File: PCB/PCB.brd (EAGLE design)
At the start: 215 parts, among them J3 Boot, Q1 FS8205A, U1 ESP32-S3HOLE

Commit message: Created the Led hole for keys library.
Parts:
- added U$97: WS2812B, Led-WS2812B:WS2812B
- moved LED1 3.80 mm to (358.8, 109.9)
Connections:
- new net LED_GND: U$97.GND
- new net LED_VDD: U$97.VDD
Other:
- board outline added: 428.5 x 124 mm
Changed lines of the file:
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@@
 <circle x="412.745" y="48.175" radius="2" width="0.001" layer="48"/>
 <circle x="428" y="48.175" radius="1.5" width="0.001" layer="48"/>
+<wire x1="4.5" y1="127" x2="429" y2="127" width="0.01" layer="20"/>
+<wire x1="431" y1="125" x2="431" y2="5" width="0.01" layer="20"/>
+<wire x1="4.6" y1="3" x2="2.5" y2="5" width="0.01" layer="20" curve="-92.862405"/>
+<wire x1="2.5" y1="5" x2="2.5" y2="125" width="0.01" layer="20"/>
+<wire x1="2.5" y1="125" x2="4.5" y2="127" width="0.01" layer="20" curve="-90"/>
+<wire x1="429" y1="127" x2="431" y2="125" width="0.01" layer="20" curve="-90"/>
+<wire x1="431" y1="5" x2="429" y2="3" width="0.01" layer="20" curve="-90"/>
+<wire x1="429" y1="3" x2="4.6" y2="3" width="0.01" layer="20"/>
 </plain>
 <attributes>
@@
 <attribute name="VALUE" x="308.85" y="107.123" size="1.27" layer="27" align="top-left"/>
 </element>
-<element name="LED1" library="SMD5050 LED" package="LED5050_W" value="" x="355" y="110" smashed="yes">
-<attribute name="NAME" x="353.095" y="112.894" size="0.8128" layer="25" ratio="18"/>
-<attribute name="VALUE" x="353.222" y="106.625" size="0.4064" layer="27" ratio="10"/>
+<element name="LED1" library="SMD5050 LED" package="LED5050_W" value="" x="358.8" y="109.9" smashed="yes">
+<attribute name="NAME" x="356.895" y="112.794" size="0.8128" layer="25" ratio="18"/>
+<attribute name="VALUE" x="357.022" y="106.525" size="0.4064" layer="27" ratio="10"/>
 </element>
 <element name="USB" library="con-headers-jp" package="SIP-100-04-32" value="F-1X04-SIP-100-32" x="375" y="115" smashed="yes" rot="R90">
@@
 <attribute name="PROD_ID" value="RES-12181" x="-18" y="-51.7" size="1.778" layer="27" display="off"/>
 <attribute name="VALUE" x="-18" y="-52.716" size="0.6096" layer="27" font="vector" ratio="20" align="top-center"/>
+</element>
+<element name="U$97" library="Led-WS2812B" package="WS2812B" value="WS2812B" x="367.5" y="103.8" smashed="yes">
+<attribute name="NAME" x="366.4" y="102.2" size="0.254" layer="25"/>
+<attribute name="VALUE" x="366.4" y="105.2" size="0.254" layer="25"/>
 </element>
 </elements>
@@
 <contactref element="U$94" pad="18"/>
 <contactref element="U$94" pad="19"/>
-<wire x1="335.4488" y1="114.8606" x2="352.3" y2="111.65" width="0" layer="19" extent="1-1"/>
+<wire x1="335.4488" y1="114.8606" x2="356.1" y2="111.55" width="0" layer="19" extent="1-1"/>
 <wire x1="335.95" y1="123.1" x2="335.4488" y2="114.8606" width="0" layer="19" extent="1-1"/>
 <wire x1="319.355" y1="114.465" x2="335.4488" y2="114.8606" width="0" layer="19" extent="1-1"/>
@@
 <contactref element="USB" pad="1"/>
 </signal>
+<signal name="LED_VDD">
+<contactref element="U$97" pad="VDD"/>
+</signal>
+<signal name="LED_GND">
+<contactref element="U$97" pad="GND"/>
+</signal>
 </signals>

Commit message: Make the connections for the Battery and Power circuits
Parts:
- removed LED1: (no value), SMD5050 LED:LED5050_W
- removed U$97: WS2812B, Led-WS2812B:WS2812B
- added BATTERY: F-1X02-SIP-100-40, con-headers-jp:SIP-100-02-40
- C1, C2, C3: value RDE5C1H273J2M1H03A -> 1uF
- moved C3 459.5 mm to (418.9, 101.9), flipped to the bottom, turned to 180 degrees
- moved R3 455.3 mm to (411.8, 98.5), turned to 180 degrees
- moved R2 451.8 mm to (402.3, 117.8), turned to 90 degrees
- moved C2 449.2 mm to (409.9, 107.4), flipped to the bottom
- moved R1 445.4 mm to (400.5, 108.4), turned to 180 degrees
- moved Q1 444.3 mm to (416.5, 117.0), flipped to the bottom, turned to 180 degrees
- moved U$95 442.2 mm to (418.8, 109.5), flipped to the bottom, turned to 180 degrees
- moved C1 436.0 mm to (401.0, 101.9), flipped to the bottom, turned to 180 degrees
- moved U$96 435.9 mm to (407.8, 116.9), flipped to the bottom, turned to 180 degrees
- moved U1 82.0 mm to (330.0, 114.0)
- moved USB 43.7 mm to (417.9, 123.1), turned to 0 degrees
- moved R5 25.9 mm to (356.2, 109.8)
- moved BUTTON 10.6 mm to (348.9, 109.7), turned to 90 degrees
- moved U$94 8.54 mm to (306.7, 112.1)
- moved J3 8.40 mm to (350.7, 122.9), turned to 180 degrees
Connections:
- removed net INGND: USB.1
- removed net LED_GND: U$97.GND
- removed net LED_VDD: U$97.VDD
- removed net VDD: LED1.1-VDD
- new net B-: BATTERY.1, C2.1, Q1.2, Q1.3, U$96.6
- new net CHRG: U$95.7
- new net N$31: R1.P$1, U$95.2
- new net N$32: R2.P$2, U$96.2
- new net N$33: Q1.5, U$96.3
- new net N$34: Q1.4, U$96.1
- new net N$36: C2.2, R3.P$2, U$96.5
- new net STDBY: U$95.6
- net GND: now also C1.1, C3.1, Q1.6, Q1.7, R1.P$2, R2.P$1, U$95.1, U$95.3, USB.1; no longer LED1.3-GND
- net INVCC: now also C1.2, U$95.4, U$95.8
- net VCC: now also BATTERY.2, C3.2, R3.P$1, U$95.5

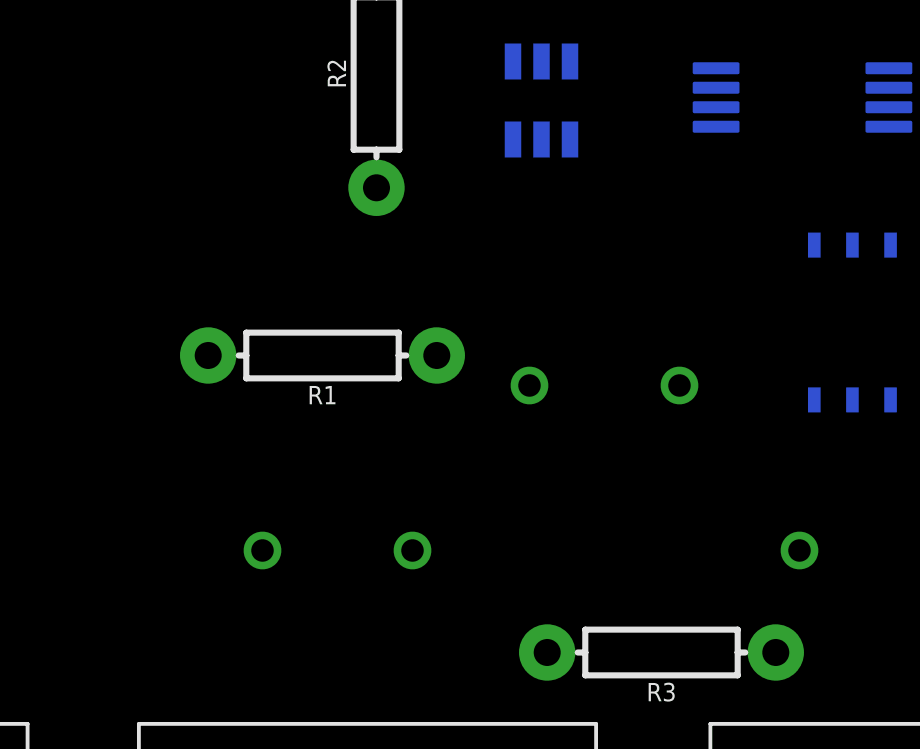
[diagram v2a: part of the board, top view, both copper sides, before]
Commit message: Make the screen DXF and added it to .pcb board
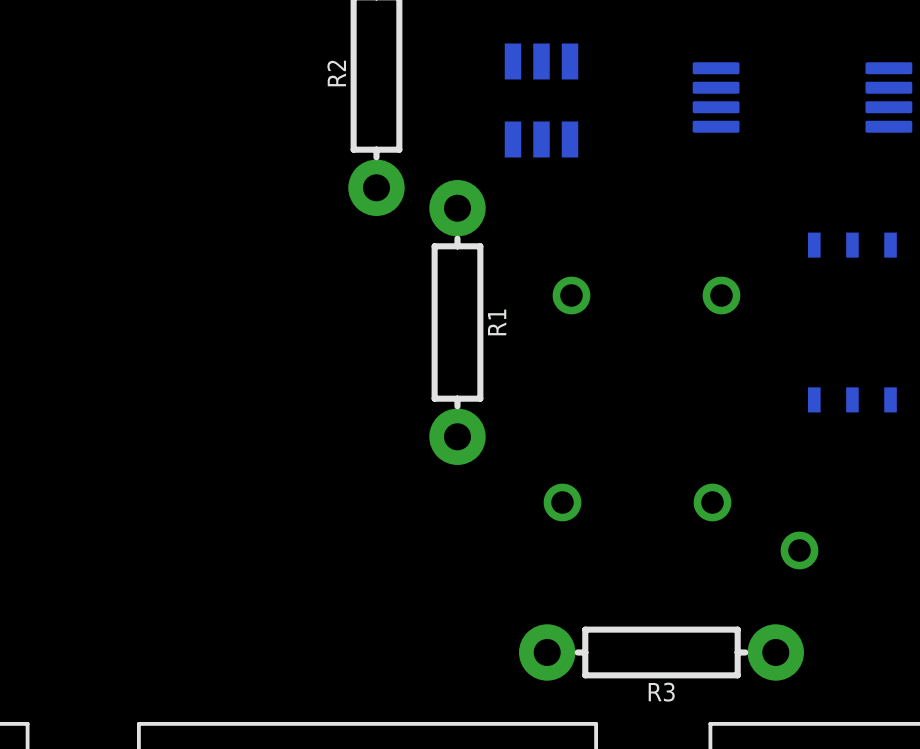
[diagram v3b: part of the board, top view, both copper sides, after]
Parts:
- moved C1 10.1 mm to (411.0, 103.5)
- moved R1 4.63 mm to (405.0, 109.5), turned to 270 degrees
- moved C2 3.31 mm to (411.3, 110.4)

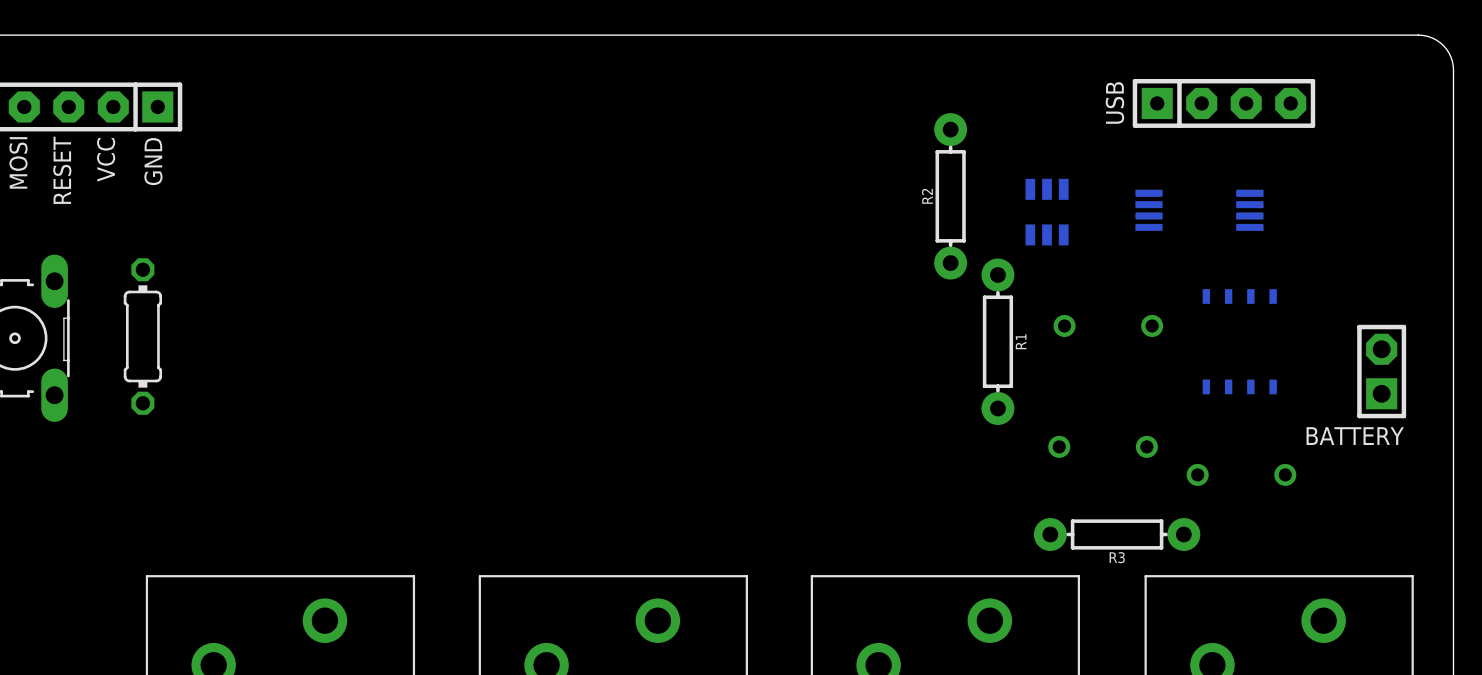
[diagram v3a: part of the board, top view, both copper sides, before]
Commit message: Changed Capacitor and resistor type
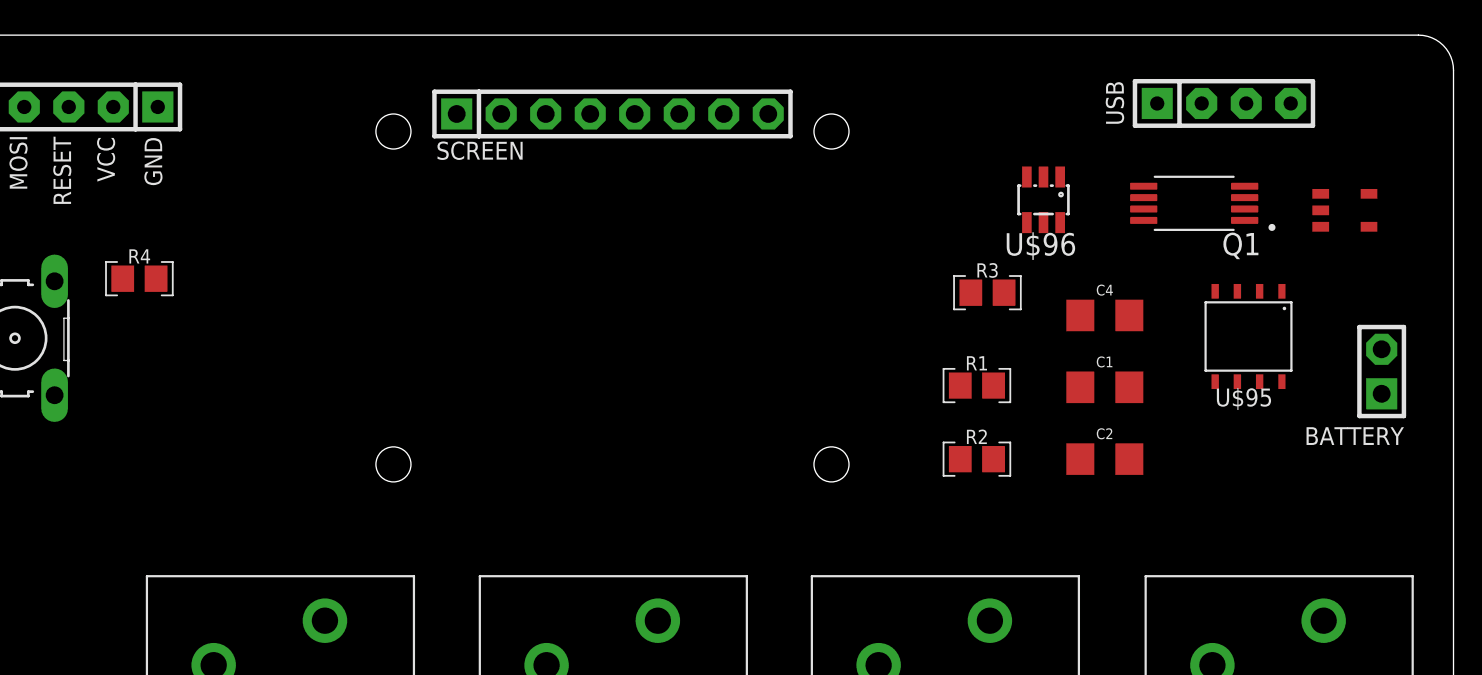
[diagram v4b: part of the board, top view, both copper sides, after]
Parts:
- removed C3: 1uF, Capacitor:CAP_RDE5C1H273J2M1H03A
- removed R5: 10K, rcl:0204/7
- added C4: 1.0uF, SparkFun-Capacitors:1206
- added R4: 1K, resistors:R-0805
- added REGULATOR: RT9080-33GJ5, RT9080:TSOT-23-5_RIT
- added SCREEN: F-1X08-SIP-100-40, con-headers-jp:SIP-100-08-40
- C1, C2: value 1uF -> 1.0uF; device Capacitor:CAP_RDE5C1H273J2M1H03A -> SparkFun-Capacitors:1206
- R1, R2, R3: value 1k -> 1K; device SparkFun-Resistors:AXIAL-0.3EZ -> resistors:R-0805
- moved R3 15.7 mm to (404.4, 112.3), turned to 0 degrees
- moved R2 15.1 mm to (403.8, 102.8), turned to 0 degrees
- moved C2 7.60 mm to (411.1, 102.8), flipped to the top
- moved C1 3.40 mm to (411.1, 106.9), flipped to the top, turned to 0 degrees
- moved R1 2.77 mm to (403.8, 107.0), turned to 0 degrees
- moved U$96 0.73 mm to (407.6, 117.6), flipped to the top
- moved U$95 0.58 mm to (419.3, 109.8), flipped to the top
- moved Q1 0.50 mm to (416.2, 117.4), flipped to the top
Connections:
- new net VIN: REGULATOR.1
- net B-: now also C2.2; no longer C2.1
- net GND: now also C1.2, C4.2, R1.2, R3.2; no longer C1.1, C3.1, R1.P$2, R2.P$1
- net INVCC: now also C4.1; no longer C1.2
- net N$31: now also R1.1; no longer R1.P$1
- net N$32: now also R3.1; no longer R2.P$2
- net N$36: now also C2.1, R2.1; no longer C2.2, R3.P$2
- net RESET: now also R4.2; no longer R5.2
- net VCC: now also C1.1, R2.2, R4.1; no longer C3.2, R3.P$1, R5.1

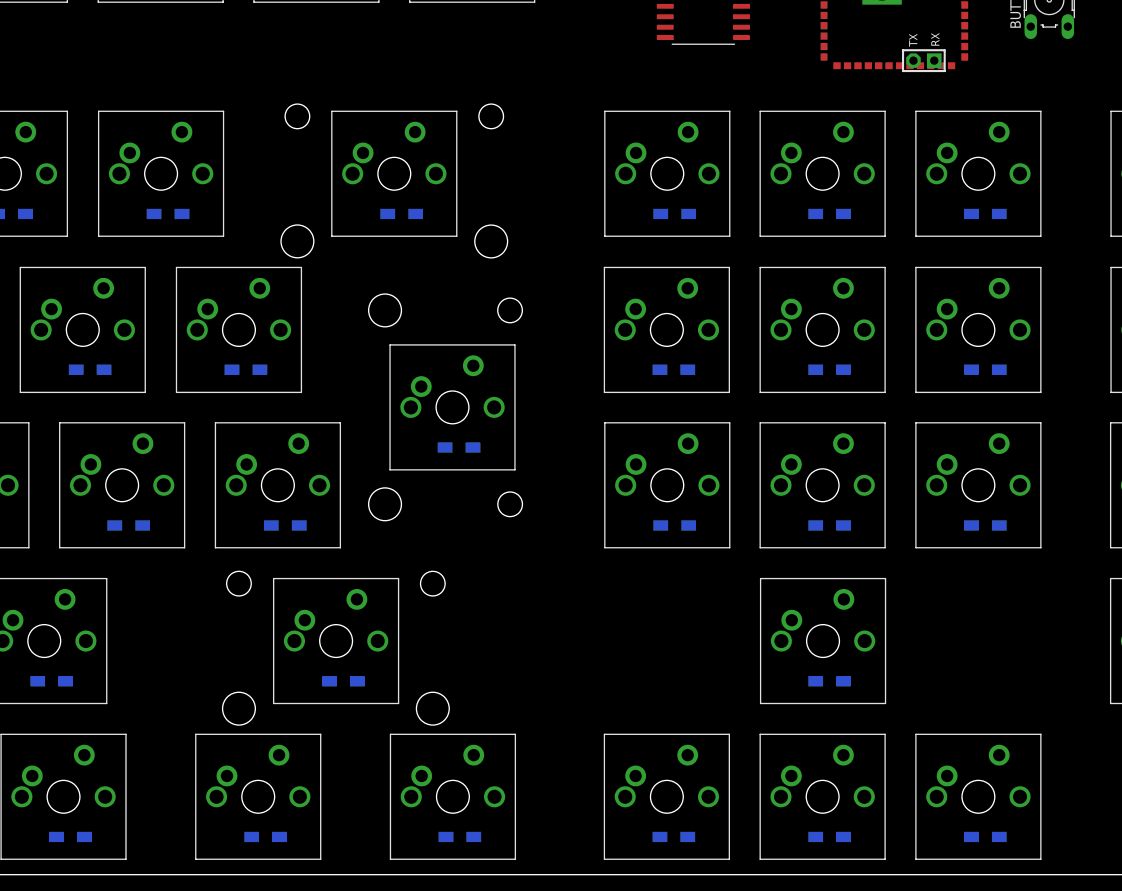
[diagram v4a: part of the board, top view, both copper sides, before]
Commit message: Added the esp32 chip connections lines in .sch
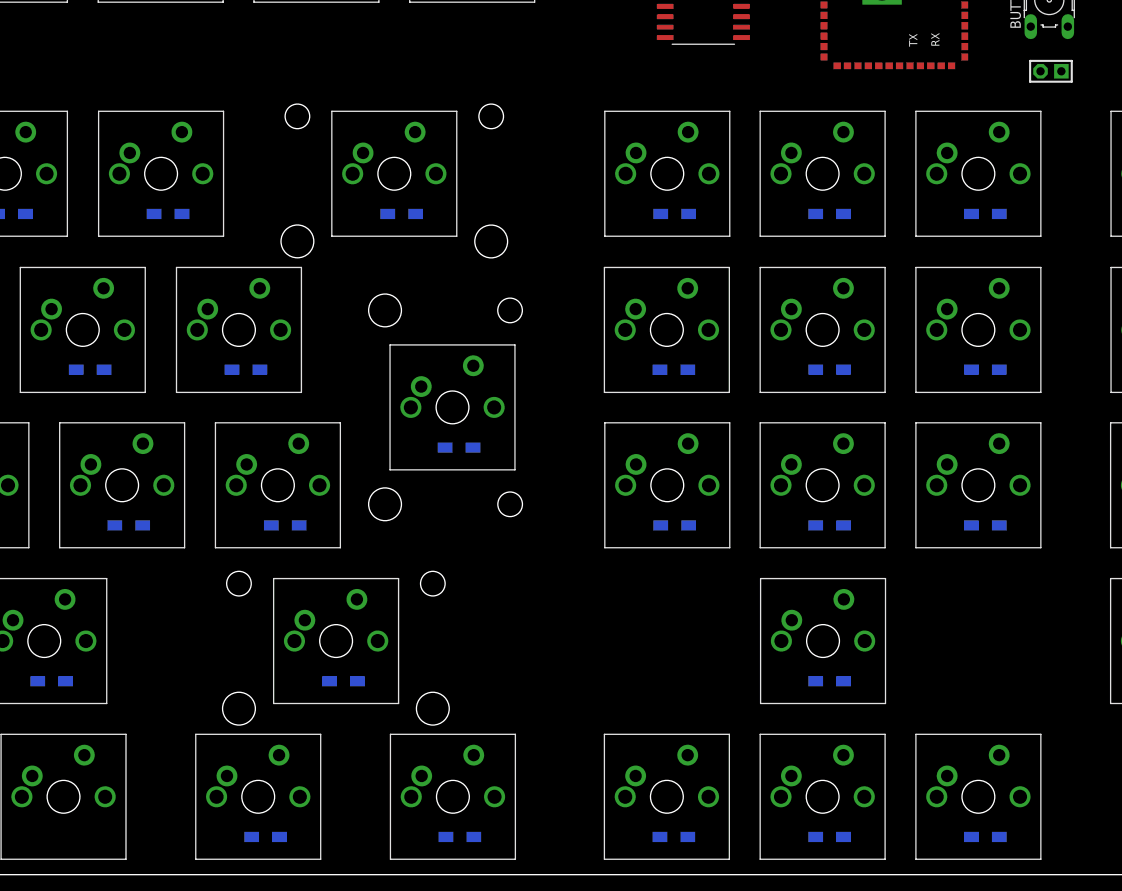
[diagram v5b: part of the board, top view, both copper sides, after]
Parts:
- removed D89: (no value), bt_diode:SOD123FL
- moved RXTX 15.6 mm to (349.1, 101.0)
- renumbered U$67 to FN_KEY
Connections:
- removed net 3V3: U1.2
- removed net N$79: D89.C, FN_KEY.SW2
- new net BATLEVEL: U1.39
- new net BLK: SCREEN.8, U1.24
- new net CS: SCREEN.7, U1.31
- new net DC: SCREEN.6, U1.32
- new net EN: U1.3
- new net KEY_FN: FN_KEY.SW2, U1.18
- new net LEDS: U1.25
- new net PROG: U1.27
- new net RES: SCREEN.5, U1.33
- new net SCL: SCREEN.3, U1.35
- new net SDA: SCREEN.4, U1.34
- net CHRG: now also U1.38
- net COD0: now also U1.4
- net COD1: now also U1.5
- net COD2: now also U1.6
- net COD3: now also U1.7
- net E0: now also U1.8
- net E1: now also U1.9
- net E2: now also U1.10
- net E3: now also U1.11
- net E4: now also U1.12
- net E5: now also U1.17; no longer D89.A
- net GND: now also FN_KEY.SW1, SCREEN.1, U1.1, U1.40, U1.41
- net MUX11: no longer FN_KEY.SW1
- net RX: now also U1.36
- net TX: now also U1.37
- net VCC: now also SCREEN.2, U1.2
